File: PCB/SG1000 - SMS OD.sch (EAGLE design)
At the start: 18 parts, among them U1A SN74AHCT125N, U2A SN74AHCT125N, U3A SN74AHCT125N

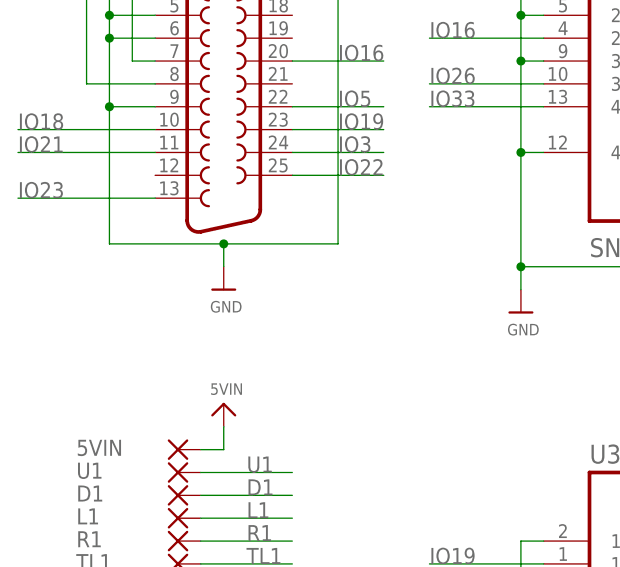
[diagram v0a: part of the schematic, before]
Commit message: Added exposed GND plane at DB25 anchors
All PCBs have been update to have exposed GND plane pads for the DB25 anchor points.

This resolves Issue 54
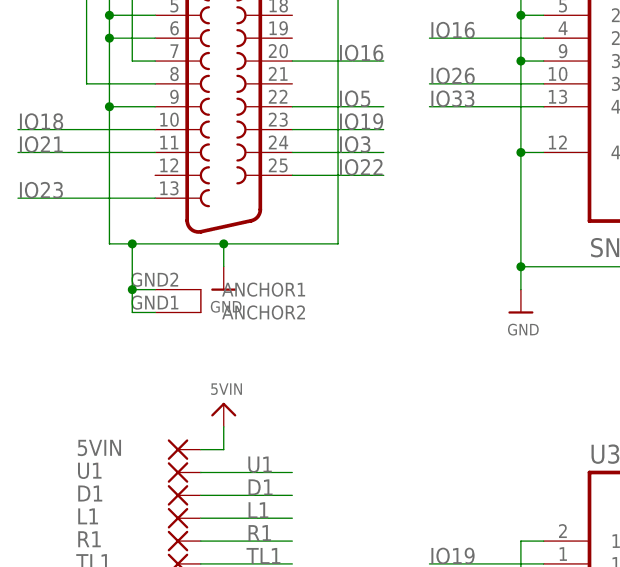
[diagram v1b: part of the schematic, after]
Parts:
- X1: device SparkFun-Retired:DB25_FEMALEH -> SparkFun-Retired:DB25_FEMALEHP
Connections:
- net GND: now also X1.ANCHOR1, X1.ANCHOR2
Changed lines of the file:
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@@
 </classes>
 <parts>
-<part name="X1" library="SparkFun-Retired" deviceset="DB25_FEMALE" device="H"/>
+<part name="X1" library="SparkFun-Retired" deviceset="DB25_FEMALE" device="HP"/>
 <part name="U$44" library="microbuilder" deviceset="VIN" device="" value="5VIN"/>
 <part name="U$45" library="Airquality_Sensor" library_urn="urn:adsk.eagle:library:16015176" deviceset="GND" device=""/>
@@
 <wire x1="238.76" y1="-109.22" x2="238.76" y2="-111.76" width="0.1524" layer="91"/>
 <junction x="238.76" y="-109.22"/>
-<wire x1="238.76" y1="-109.22" x2="226.06" y2="-109.22" width="0.1524" layer="91"/>
+<wire x1="238.76" y1="-109.22" x2="228.6" y2="-109.22" width="0.1524" layer="91"/>
+<wire x1="228.6" y1="-109.22" x2="226.06" y2="-109.22" width="0.1524" layer="91"/>
 <wire x1="226.06" y1="-81.28" x2="226.06" y2="-83.82" width="0.1524" layer="91"/>
 <wire x1="226.06" y1="-83.82" x2="226.06" y2="-86.36" width="0.1524" layer="91"/>
@@
 <wire x1="226.06" y1="-78.74" x2="226.06" y2="-81.28" width="0.1524" layer="91"/>
 <junction x="226.06" y="-81.28"/>
+<pinref part="X1" gate="-1" pin="ANCHOR2"/>
+<wire x1="231.14" y1="-116.84" x2="228.6" y2="-116.84" width="0.1524" layer="91"/>
+<wire x1="228.6" y1="-116.84" x2="228.6" y2="-114.3" width="0.1524" layer="91"/>
+<junction x="228.6" y="-109.22"/>
+<pinref part="X1" gate="-1" pin="ANCHOR1"/>
+<wire x1="228.6" y1="-114.3" x2="228.6" y2="-109.22" width="0.1524" layer="91"/>
+<wire x1="231.14" y1="-114.3" x2="228.6" y2="-114.3" width="0.1524" layer="91"/>
+<junction x="228.6" y="-114.3"/>
 </segment>
 <segment>
